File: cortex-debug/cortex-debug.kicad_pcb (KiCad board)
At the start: 2 copper layers, 27 x 24 mm, 6 parts, among them J1 SALEAE_0-3, J2 SALEAE_0-3, J5 SALEAE_4-7, J6 SALEAE_4-7, P1 SWD, P2 SWD

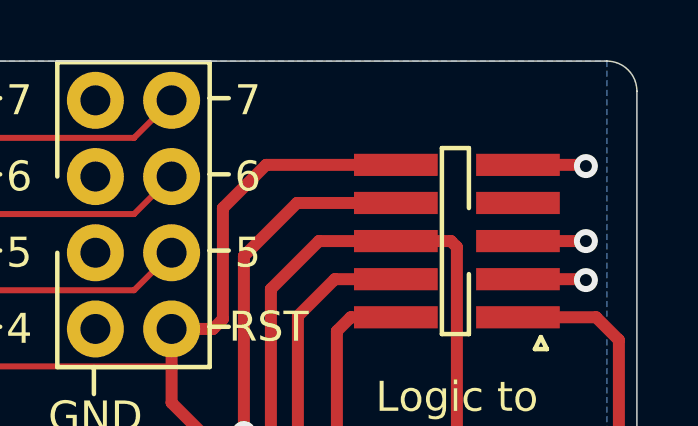
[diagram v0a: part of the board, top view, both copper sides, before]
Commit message: Update with silk date/rev code
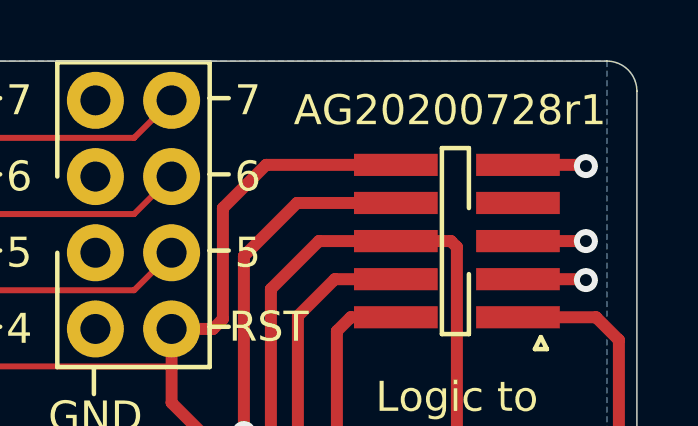
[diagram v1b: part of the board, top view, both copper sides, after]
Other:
- board text added: "AG20200728r1"
